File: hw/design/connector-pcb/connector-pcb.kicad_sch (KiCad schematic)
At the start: 5 parts, among them J1 B04B-JWPF-SK-R, J2 PinHeader (2.54mm), SW1 KSC421G70

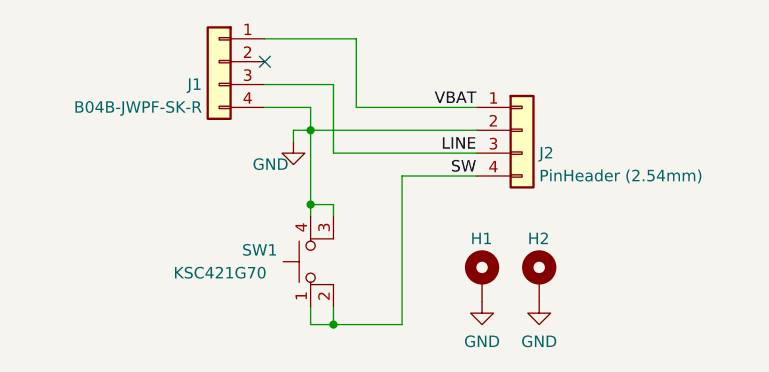
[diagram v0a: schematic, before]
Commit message: Hardware schematic cleanup
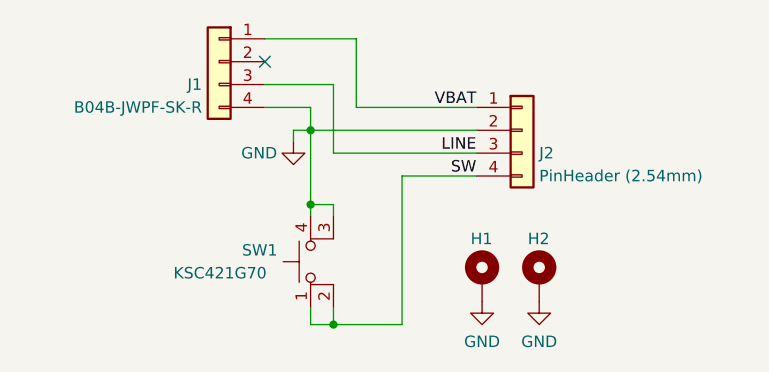
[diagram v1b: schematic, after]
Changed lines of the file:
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@@
       (effects (font (size 1.27 1.27)) hide)
     )
-    (property "Value" "GND" (at 131.445 91.44 0)
+    (property "Value" "GND" (at 130.175 90.17 0)
       (effects (font (size 1.27 1.27)))
     )

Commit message: Connector board modified to use the 3pin connector
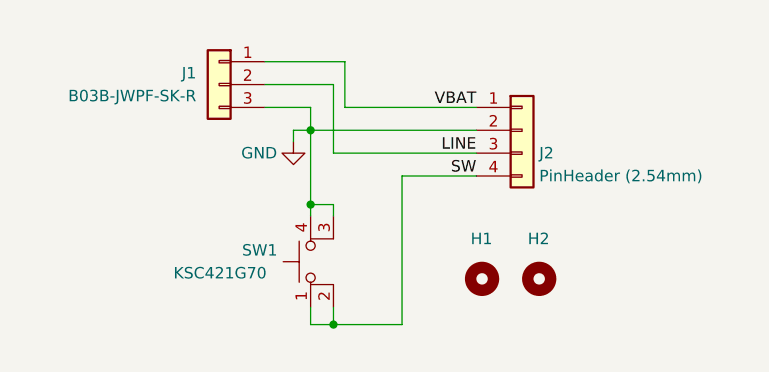
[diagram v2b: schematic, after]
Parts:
- H1, H2: symbol Mechanical:MountingHole_Pad -> Mechanical:MountingHole
- J1: value B04B-JWPF-SK-R -> B03B-JWPF-SK-R; footprint Connector_JST:JST_JWPF_B04B-JWPF-SK-R_1x04_P2.00mm_Vertical -> Connector_JST:JST_JWPF_B03B-JWPF-SK-R_1x03_P2.00mm_Vertical; symbol Connector_Generic:Conn_01x04 -> Connector_Generic:Conn_01x03
- J2: footprint Connector_PinHeader_2.00mm:PinHeader_2x02_P2.00mm_Vertical_SMD -> Connector_PinHeader_2.00mm:PinHeader_1x04_P2.00mm_Vertical_SMD_Pin1Left
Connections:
- net GND: now also J1.3 (Pin_3); no longer H1.1, H2.1, J1.4 (Pin_4)
- net LINE: now also J1.2 (Pin_2); no longer J1.3 (Pin_3)
- no-connect marks 1 -> 0
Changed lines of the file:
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@@
   (junction (at 135.89 95.885) (diameter 0) (color 0 0 0 0)
   )
-  (no_connect (at 130.81 80.01))
   (wire (pts (xy 135.89 109.22) (xy 138.43 109.22))
     (stroke (width 0) (type default))
@@
     (stroke (width 0) (type default))
   )
-  (wire (pts (xy 140.97 77.47) (xy 140.97 85.09))
+  (wire (pts (xy 139.7 80.01) (xy 139.7 85.09))
     (stroke (width 0) (type default))
   )
@@
     (stroke (width 0) (type default))
   )
-  (wire (pts (xy 130.81 77.47) (xy 140.97 77.47))
+  (wire (pts (xy 130.81 80.01) (xy 139.7 80.01))
     (stroke (width 0) (type default))
   )
@@
     (stroke (width 0) (type default))
   )
-  (wire (pts (xy 140.97 85.09) (xy 154.305 85.09))
+  (wire (pts (xy 139.7 85.09) (xy 154.305 85.09))
     (stroke (width 0) (type default))
   )
@@
   (label "LINE" (at 154.305 90.17 180) (fields_autoplaced)
     (effects (font (size 1.27 1.27)) (justify right bottom))
-  )
-  (symbol (lib_id "power:GND") (at 161.29 106.68 0) (unit 1)
-    (in_bom yes) (on_board yes) (dnp no) (fields_autoplaced)
-    (property "Reference" "#PWR02" (at 161.29 113.03 0)
-      (effects (font (size 1.27 1.27)) hide)
-    )
-    (property "Value" "GND" (at 161.29 111.125 0)
-      (effects (font (size 1.27 1.27)))
-    )
-    (property "Footprint" "" (at 161.29 106.68 0)
-      (effects (font (size 1.27 1.27)) hide)
-    )
-    (property "Datasheet" "" (at 161.29 106.68 0)
-      (effects (font (size 1.27 1.27)) hide)
-    )
-    (pin "1")
-    (instances
-      (project "connector-pcb"
-        (path "/7681db4b-9d05-4784-b7a7-2c8f73623790"
-          (reference "#PWR02") (unit 1)
-        )
-      )
-    )
   )
   (symbol (lib_id "power:GND") (at 133.985 88.9 0) (unit 1)
@@
     )
   )
-  (symbol (lib_id "Mechanical:MountingHole_Pad") (at 154.94 104.14 0) (unit 1)
+  (symbol (lib_id "Mechanical:MountingHole") (at 154.94 104.14 0) (unit 1)
     (in_bom yes) (on_board yes) (dnp no)
     (property "Reference" "H1" (at 153.67 99.695 0)
@@
       (effects (font (size 1.27 1.27)) hide)
     )
-    (pin "1")
     (instances
       (project "connector-pcb"
@@
     )
   )
-  (symbol (lib_id "Mechanical:MountingHole_Pad") (at 161.29 104.14 0) (unit 1)
+  (symbol (lib_id "Mechanical:MountingHole") (at 161.29 104.14 0) (unit 1)
     (in_bom yes) (on_board yes) (dnp no)
     (property "Reference" "H2" (at 160.02 99.695 0)
@@
       (effects (font (size 1.27 1.27)) hide)
     )
-    (pin "1")
     (instances
       (project "connector-pcb"
@@
       (effects (font (size 1.27 1.27)) (justify left))
     )
-    (property "Footprint" "Connector_PinHeader_2.00mm:PinHeader_2x02_P2.00mm_Vertical_SMD" (at 159.385 87.63 0)
+    (property "Footprint" "Connector_PinHeader_2.00mm:PinHeader_1x04_P2.00mm_Vertical_SMD_Pin1Left" (at 159.385 87.63 0)
       (effects (font (size 1.27 1.27)) hide)
     )
@@
     )
   )
-  (symbol (lib_id "Connector_Generic:Conn_01x04") (at 125.73 80.01 0) (mirror y) (unit 1)
+  (symbol (lib_id "Connector_Generic:Conn_01x03") (at 125.73 82.55 0) (mirror y) (unit 1)
     (in_bom yes) (on_board yes) (dnp no)
-    (property "Reference" "J1" (at 123.825 82.55 0)
+    (property "Reference" "J1" (at 123.19 81.28 0)
       (effects (font (size 1.27 1.27)) (justify left))
     )
-    (property "Value" "B04B-JWPF-SK-R" (at 123.825 85.09 0)
+    (property "Value" "B03B-JWPF-SK-R" (at 123.19 83.82 0)
       (effects (font (size 1.27 1.27)) (justify left))
     )
-    (property "Footprint" "Connector_JST:JST_JWPF_B04B-JWPF-SK-R_1x04_P2.00mm_Vertical" (at 125.73 80.01 0)
+    (property "Footprint" "Connector_JST:JST_JWPF_B03B-JWPF-SK-R_1x03_P2.00mm_Vertical" (at 125.73 82.55 0)
       (effects (font (size 1.27 1.27)) hide)
     )
-    (property "Datasheet" "~" (at 125.73 80.01 0)
+    (property "Datasheet" "~" (at 125.73 82.55 0)
       (effects (font (size 1.27 1.27)) hide)
     )
@@
     (pin "2")
     (pin "3")
-    (pin "4")
     (instances
       (project "connector-pcb"
@@
         )
       )
-    )
-  )
-  (symbol (lib_id "power:GND") (at 154.94 106.68 0) (unit 1)
-    (in_bom yes) (on_board yes) (dnp no) (fields_autoplaced)
-    (property "Reference" "#PWR01" (at 154.94 113.03 0)
-      (effects (font (size 1.27 1.27)) hide)
-    )
-    (property "Value" "GND" (at 154.94 111.125 0)
-      (effects (font (size 1.27 1.27)))
-    )
-    (property "Footprint" "" (at 154.94 106.68 0)
-      (effects (font (size 1.27 1.27)) hide)
-    )
-    (property "Datasheet" "" (at 154.94 106.68 0)
-      (effects (font (size 1.27 1.27)) hide)
-    )
-    (pin "1")
-    (instances
-      (project "connector-pcb"
-        (path "/7681db4b-9d05-4784-b7a7-2c8f73623790"
-          (reference "#PWR01") (unit 1)
-        )
-      )
